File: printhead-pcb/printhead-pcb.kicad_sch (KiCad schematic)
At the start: 29 parts, among them J1 Power, J18 DATA, U1 PCA9615DP, U6 AP7361C-33E

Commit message: implemented custom footprint
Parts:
- J1: footprint Connector_JST:JST_EH_S3B-EH_1x03_P2.50mm_Horizontal -> CustomFotLibByJan:CONN4_S4B-XH_JST
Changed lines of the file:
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@@
 			)
 		)
-		(property "Footprint" "Connector_JST:JST_EH_S3B-EH_1x03_P2.50mm_Horizontal"
+		(property "Footprint" "CustomFotLibByJan:CONN4_S4B-XH_JST"
 			(at 17.78 27.94 0)
 			(effects

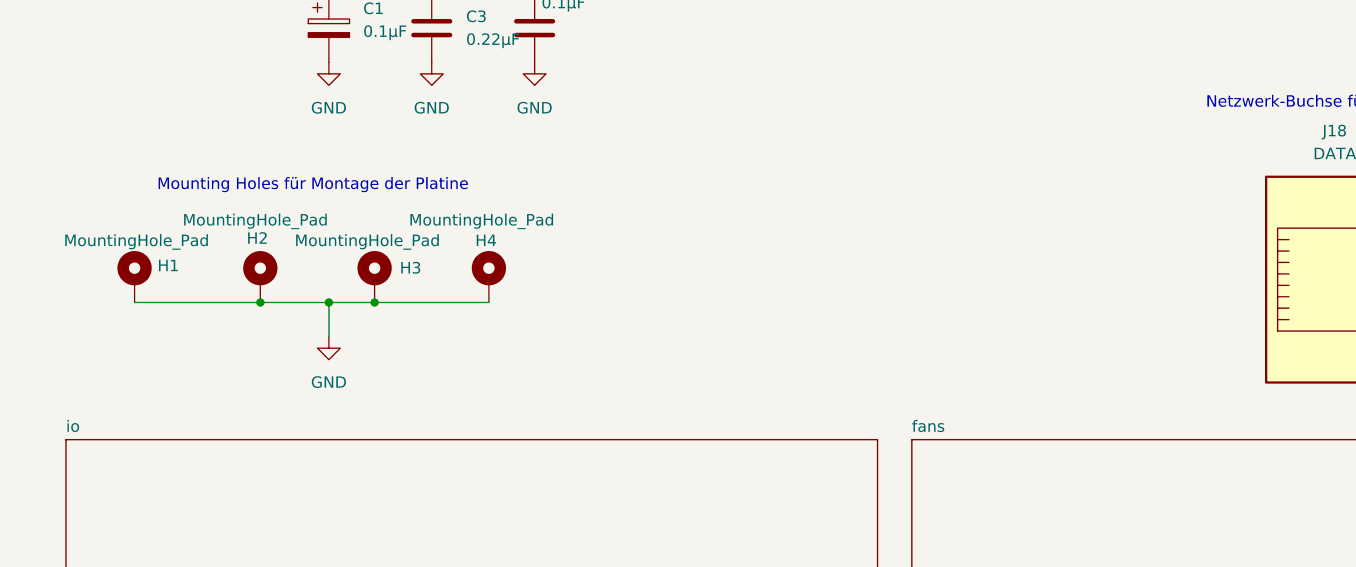
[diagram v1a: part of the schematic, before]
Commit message: added new sheet for stacked pcb
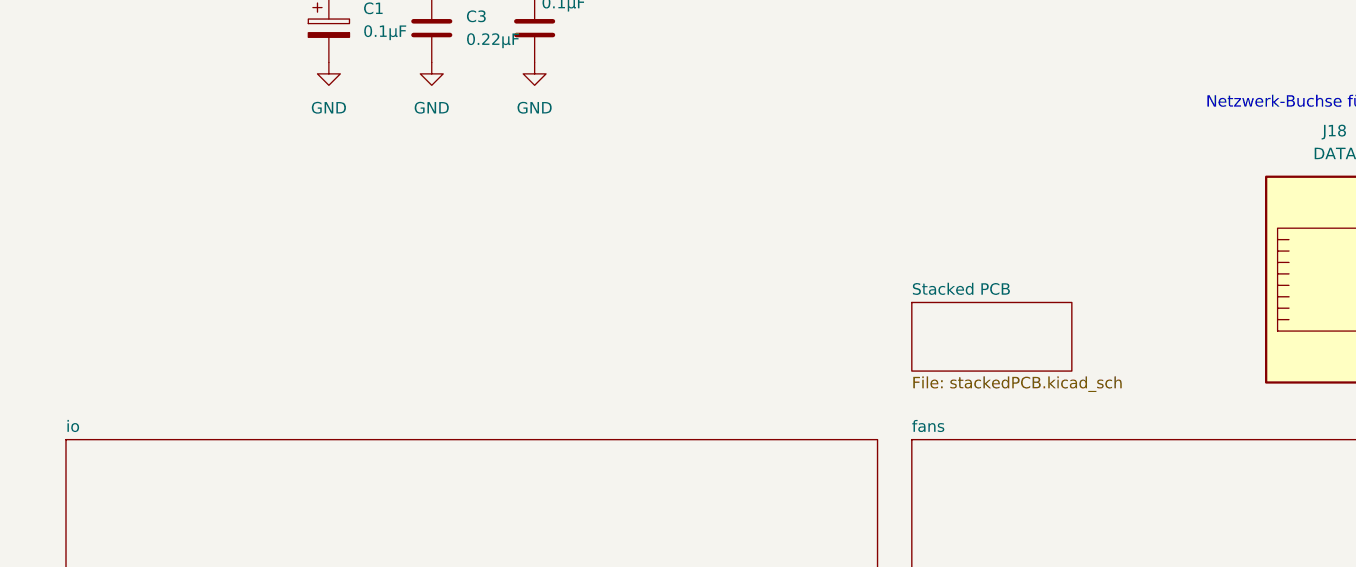
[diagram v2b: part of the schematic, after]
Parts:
- removed H1, H2, H3, H4: MountingHole_Pad, MountingHole:MountingHole_2.2mm_M2_Pad_TopBottom, symbol Mechanical:MountingHole_Pad
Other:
- added sheet Stacked PCB (stackedPCB.kicad_sch)
- note removed: "Mounting Holes für Montage der Platine"
